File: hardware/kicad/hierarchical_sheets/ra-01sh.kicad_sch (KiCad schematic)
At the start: 3 parts, among them J4 CONSMA020.062-G, U3 RA-01SH

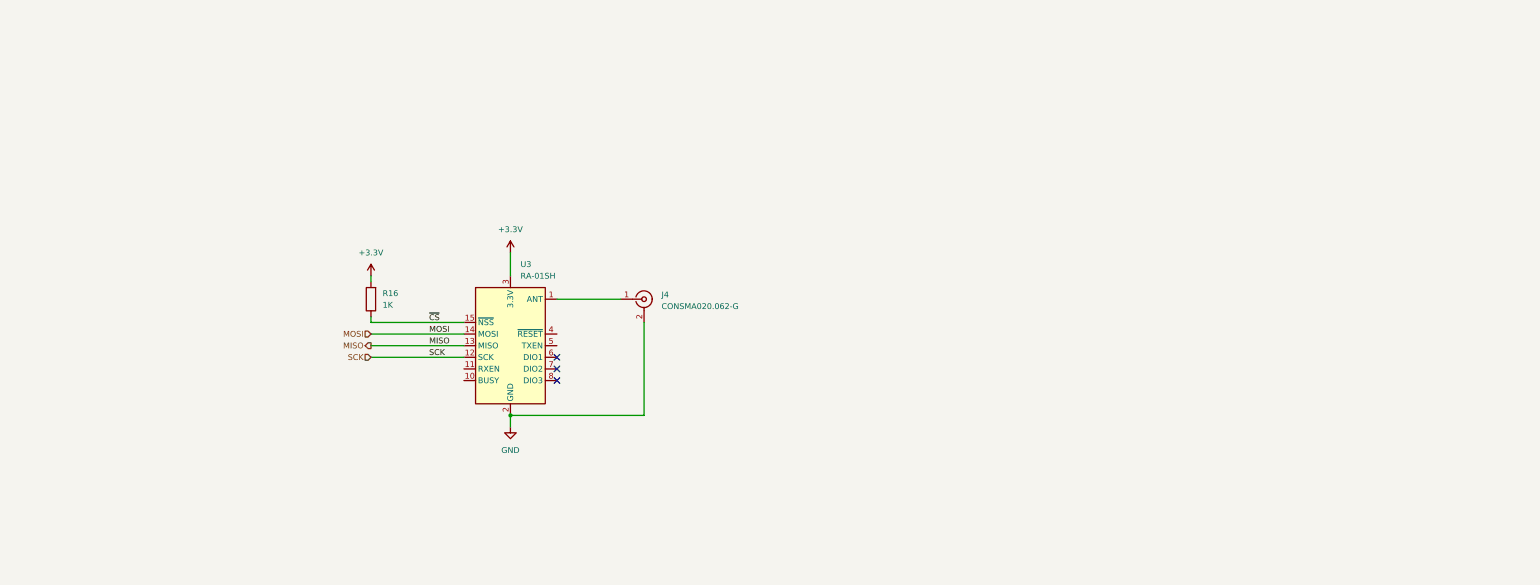
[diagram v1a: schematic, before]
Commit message: added comments to storage and telemetry radio
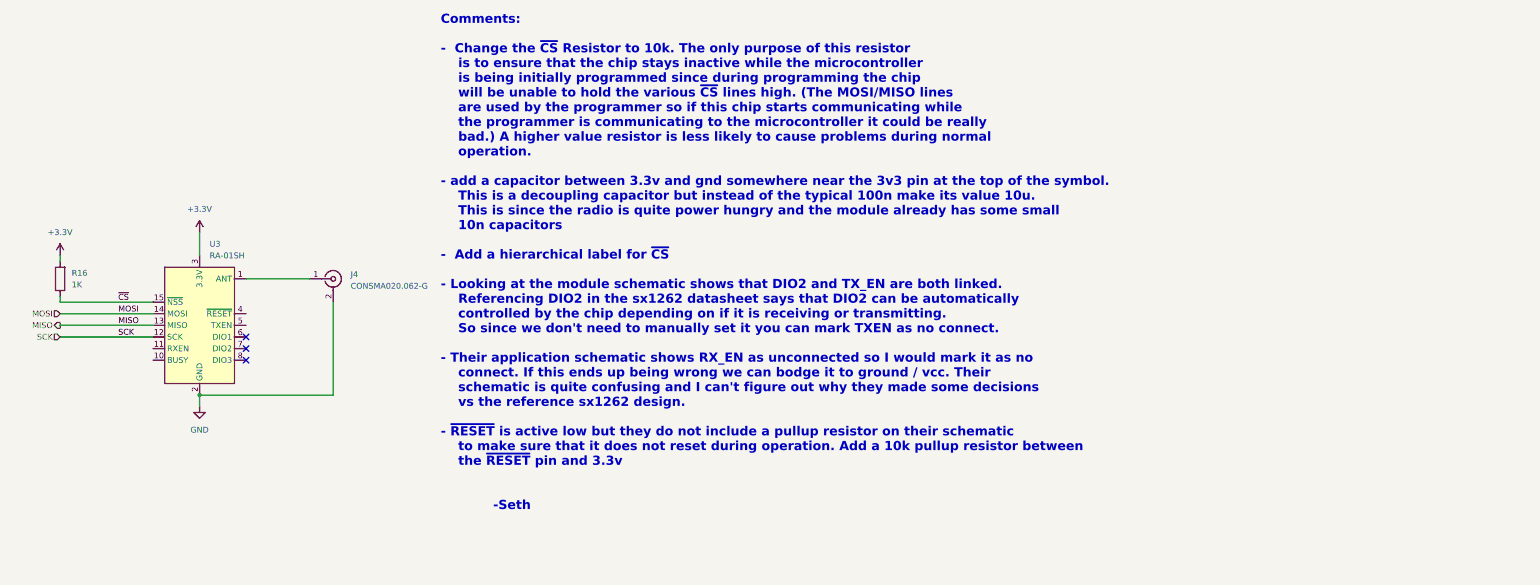
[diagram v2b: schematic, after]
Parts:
- U3: Digikey https://docs.ai-thinker.com/_media/lora/docs/ra-01sh_specif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 -> https://www.digikey.com/en/products/detail/ai-thinker/RA-01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
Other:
- note added: "Comments: - Change the ~{CS} Resistor to 10k. The only purpose of this resistor is to ensure that the chip stays inactive while the microcontroller is being initially programmed since during programming the chip will be unable to hold the various ~{CS} lines high. (The MOSI/MISO lines are used by the programmer so if this chip starts communicating while the programmer is communicating to the micr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"
- moved on the sheet: J4, R16, U3

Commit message: literally moved half the microcontroller pins :(
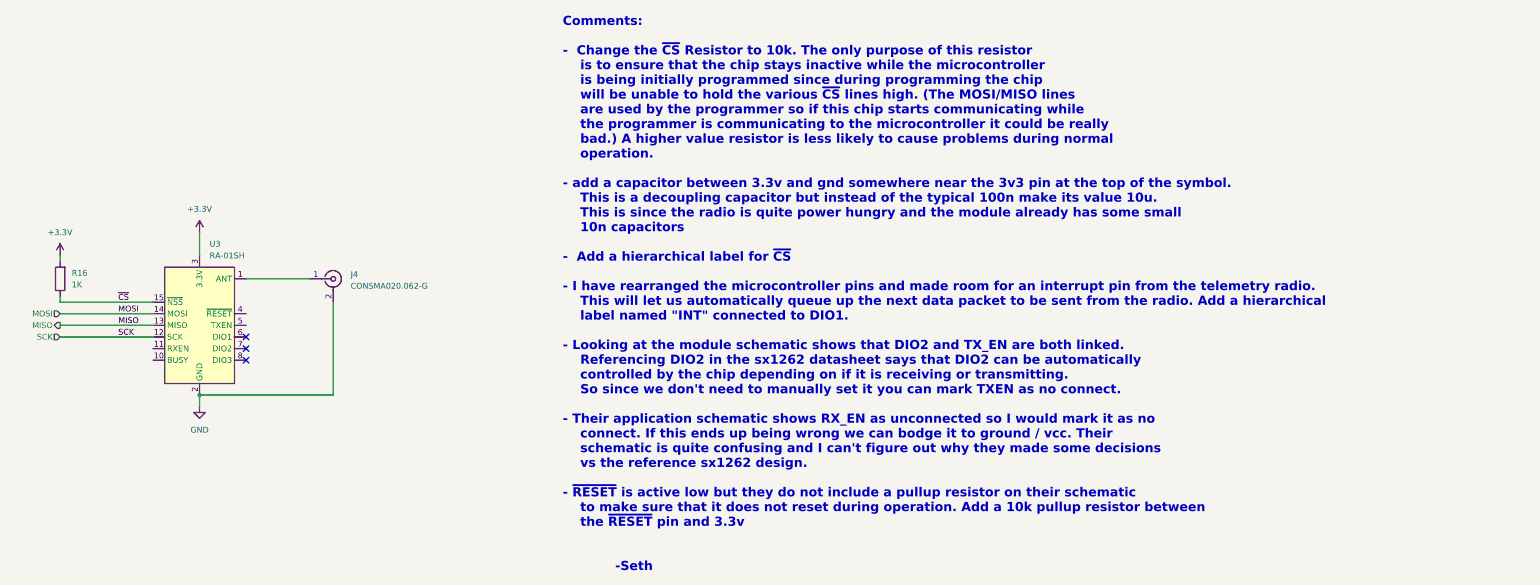
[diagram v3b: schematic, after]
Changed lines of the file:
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@@
     )
   )
-  (text "Comments:\n\n-  Change the ~{CS} Resistor to 10k. The only purpose of this resistor\n	is to ensure that the chip stays inactive while the microcontroller\n	is being initially programmed since during programming the chip\n	will be unable to hold the various ~{CS} lines high. (The MOSI/MISO lines \n	are used by the programmer so if this chip starts communicating while\n	the programmer is communicating to the microcontroller it could be really \n	bad.) A higher value resistor is less likely to cause problems during normal \n	operation. \n\n- add a capacitor between 3.3v and gnd somewhere near the 3v3 pin at the top of the symbol.\n	This is a decoupling capacitor but instead of the typical 100n make its value 10u.\n	This is since the radio is quite power hungry and the module already has some small\n	10n capacitors \n\n-  Add a hierarchical label for ~{CS} \n\n- Looking at the module schematic shows that DIO2 and TX_EN are both linked.\n	Referencing DIO2 in the sx1262 datasheet says that DIO2 can be automatically\n	controlled by the chip depending on if it is receiving or transmitting. \n	So since we don't need to manually set it you can mark TXEN as no connect. \n\n- Their application schematic shows RX_EN as unconnected so I would mark it as no \n	connect. If this ends up being wrong we can bodge it to ground / vcc. Their \n	schematic is quite confusing and I can't figure out why they made some decisions \n	vs the reference sx1262 design. \n\n- ~{RESET} is active low but they do not include a pullup resistor on their schematic\n	to make sure that it does not reset during operation. Add a 10k pullup resistor between \n	the ~{RESET} pin and 3.3v\n\n\n			-Seth"
-    (at 116.84 123.825 0)
+  (text "Comments:\n\n-  Change the ~{CS} Resistor to 10k. The only purpose of this resistor\n	is to ensure that the chip stays inactive while the microcontroller\n	is being initially programmed since during programming the chip\n	will be unable to hold the various ~{CS} lines high. (The MOSI/MISO lines \n	are used by the programmer so if this chip starts communicating while\n	the programmer is communicating to the microcontroller it could be really \n	bad.) A higher value resistor is less likely to cause problems during normal \n	operation. \n\n- add a capacitor between 3.3v and gnd somewhere near the 3v3 pin at the top of the symbol.\n	This is a decoupling capacitor but instead of the typical 100n make its value 10u.\n	This is since the radio is quite power hungry and the module already has some small\n	10n capacitors \n\n-  Add a hierarchical label for ~{CS} \n\n- I have rearranged the microcontroller pins and made room for an interrupt pin from the telemetry radio. \n	This will let us automatically queue up the next data packet to be sent from the radio. Add a hierarchical \n	label named \"INT\" connected to DIO1.\n\n- Looking at the module schematic shows that DIO2 and TX_EN are both linked.\n	Referencing DIO2 in the sx1262 datasheet says that DIO2 can be automatically\n	controlled by the chip depending on if it is receiving or transmitting. \n	So since we don't need to manually set it you can mark TXEN as no connect. \n\n- Their application schematic shows RX_EN as unconnected so I would mark it as no \n	connect. If this ends up being wrong we can bodge it to ground / vcc. Their \n	schematic is quite confusing and I can't figure out why they made some decisions \n	vs the reference sx1262 design. \n\n- ~{RESET} is active low but they do not include a pullup resistor on their schematic\n	to make sure that it does not reset during operation. Add a 10k pullup resistor between \n	the ~{RESET} pin and 3.3v\n\n\n			-Seth"
+    (at 143.51 137.16 0)
     (effects (font (size 2 2) (thickness 0.4) bold (color 255 48 0 1)) (justify left bottom))
   )

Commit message: fixed schematic RA-01SH
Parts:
- added C3: 100n, symbol Device:C
- added R22: 10k, symbol Device:R
- R16: value 1K -> 10K
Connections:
- net +3.3V: now also C3.1, R22.1
- net GND: now also C3.2
- net BUSY: now reaches U3.10 (BUSY)
- net at U3.4 (~{RESET}): now also R22.2
- net INT: now reaches U3.6 (DIO1)
- net ~{CS} renamed CS
- no-connect marks 3 -> 4
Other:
- note removed: "Comments: - Change the ~{CS} Resistor to 10k. The only purpose of this resistor is to ensure that the chip stays inactive while the microcontroller is being initially programmed since during programming the chip will be unable to hold the various ~{CS} lines high. (The MOSI/MISO lines are used by the programmer so if this chip starts communicating while the programmer is communicating to the micr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"

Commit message: Max Working Current
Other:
- note added: "Maximum Working Current is 140mA"
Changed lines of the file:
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@@
     )
+  )
+  (text "Maximum Working Current is 140mA" (at 48.26 120.65 0)
+    (effects (font (size 1.27 1.27)) (justify left bottom))
   )
   (label "MOSI" (at 46.355 80.645 0) (fields_autoplaced)

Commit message: added invert on cs
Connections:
- net CS renamed ~{CS}
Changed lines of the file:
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@@
     (effects (font (size 1.27 1.27)) (justify right))
   )
-  (hierarchical_label "CS" (shape input) (at 31.115 78.105 180) (fields_autoplaced)
+  (hierarchical_label "~{CS}" (shape input) (at 31.115 78.105 180) (fields_autoplaced)
     (effects (font (size 1.27 1.27)) (justify right))
   )

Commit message: added power and checked schematics
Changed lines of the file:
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@@
     (effects (font (size 1.27 1.27)) (justify right))
   )
-  (hierarchical_label "INT" (shape input) (at 80.01 85.725 0) (fields_autoplaced)
+  (hierarchical_label "INT" (shape output) (at 80.01 85.725 0) (fields_autoplaced)
     (effects (font (size 1.27 1.27)) (justify left))
   )

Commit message: assigned footprints
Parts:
- C7: renamed from C3; footprint (none) -> Resistor_SMD:R_0603_1608Metric
- R16: footprint (none) -> Resistor_SMD:R_0603_1608Metric
- R17: renamed from R22; footprint (none) -> Resistor_SMD:R_0603_1608Metric
- renumbered U3 to U6
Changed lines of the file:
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@@
   (symbol (lib_id "power:GND") (at 49.53 64.77 0) (unit 1)
     (in_bom yes) (on_board yes) (dnp no) (fields_autoplaced)
-    (property "Reference" "#PWR028" (at 49.53 71.12 0)
+    (property "Reference" "#PWR027" (at 49.53 71.12 0)
       (effects (font (size 1.27 1.27)) hide)
     )
@@
       (project "FC"
         (path "/54cce219-8b98-4e71-96c4-f9ee784aa3bc/35031a3a-251a-4009-92bf-5738de5c8c69"
+          (reference "#PWR027") (unit 1)
+        )
+      )
+    )
+  )
+  (symbol (lib_id "power:GND") (at 64.135 100.965 0) (unit 1)
+    (in_bom yes) (on_board yes) (dnp no) (fields_autoplaced)
+    (property "Reference" "#PWR028" (at 64.135 107.315 0)
+      (effects (font (size 1.27 1.27)) hide)
+    )
+    (property "Value" "GND" (at 64.135 106.045 0)
+      (effects (font (size 1.27 1.27)))
+    )
+    (property "Footprint" "" (at 64.135 100.965 0)
+      (effects (font (size 1.27 1.27)) hide)
+    )
+    (property "Datasheet" "" (at 64.135 100.965 0)
+      (effects (font (size 1.27 1.27)) hide)
+    )
+    (pin "1")
+    (instances
+      (project "FC"
+        (path "/54cce219-8b98-4e71-96c4-f9ee784aa3bc/35031a3a-251a-4009-92bf-5738de5c8c69"
           (reference "#PWR028") (unit 1)
         )
@@
     )
   )
-  (symbol (lib_id "power:GND") (at 64.135 100.965 0) (unit 1)
-    (in_bom yes) (on_board yes) (dnp no) (fields_autoplaced)
-    (property "Reference" "#PWR024" (at 64.135 107.315 0)
-      (effects (font (size 1.27 1.27)) hide)
-    )
-    (property "Value" "GND" (at 64.135 106.045 0)
-      (effects (font (size 1.27 1.27)))
-    )
-    (property "Footprint" "" (at 64.135 100.965 0)
-      (effects (font (size 1.27 1.27)) hide)
-    )
-    (property "Datasheet" "" (at 64.135 100.965 0)
-      (effects (font (size 1.27 1.27)) hide)
-    )
-    (pin "1")
-    (instances
-      (project "FC"
-        (path "/54cce219-8b98-4e71-96c4-f9ee784aa3bc/35031a3a-251a-4009-92bf-5738de5c8c69"
-          (reference "#PWR024") (unit 1)
-        )
-      )
-    )
-  )
   (symbol (lib_id "Device:R") (at 133.985 62.23 0) (unit 1)
     (in_bom yes) (on_board yes) (dnp no) (fields_autoplaced)
-    (property "Reference" "R22" (at 135.89 60.96 0)
+    (property "Reference" "R17" (at 135.89 60.96 0)
       (effects (font (size 1.27 1.27)) (justify left))
     )
@@
       (effects (font (size 1.27 1.27)) (justify left))
     )
-    (property "Footprint" "" (at 132.207 62.23 90)
+    (property "Footprint" "Resistor_SMD:R_0603_1608Metric" (at 132.207 62.23 90)
       (effects (font (size 1.27 1.27)) hide)
     )
@@
       (project "FC"
         (path "/54cce219-8b98-4e71-96c4-f9ee784aa3bc/35031a3a-251a-4009-92bf-5738de5c8c69"
-          (reference "R22") (unit 1)
+          (reference "R17") (unit 1)
         )
       )
@@
   (symbol (lib_id "Device:C") (at 49.53 58.42 0) (unit 1)
     (in_bom yes) (on_board yes) (dnp no) (fields_autoplaced)
-    (property "Reference" "C3" (at 53.34 57.15 0)
+    (property "Reference" "C7" (at 53.34 57.15 0)
       (effects (font (size 1.27 1.27)) (justify left))
     )
@@
       (effects (font (size 1.27 1.27)) (justify left))
     )
-    (property "Footprint" "" (at 50.4952 62.23 0)
+    (property "Footprint" "Resistor_SMD:R_0603_1608Metric" (at 50.4952 62.23 0)
       (effects (font (size 1.27 1.27)) hide)
     )
@@
       (project "FC"
         (path "/54cce219-8b98-4e71-96c4-f9ee784aa3bc/35031a3a-251a-4009-92bf-5738de5c8c69"
-          (reference "C3") (unit 1)
+          (reference "C7") (unit 1)
         )
       )
@@
   (symbol (lib_id "RA-01SH:RA-01SH") (at 64.135 83.185 0) (unit 1)
     (in_bom yes) (on_board yes) (dnp no) (fields_autoplaced)
-    (property "Reference" "U3" (at 66.3291 65.405 0)
+    (property "Reference" "U6" (at 66.3291 65.405 0)
       (effects (font (size 1.27 1.27)) (justify left))
     )
@@
       (project "FC"
         (path "/54cce219-8b98-4e71-96c4-f9ee784aa3bc/35031a3a-251a-4009-92bf-5738de5c8c69"
-          (reference "U3") (unit 1)
+          (reference "U6") (unit 1)
         )
       )
@@
       (effects (font (size 1.27 1.27)) (justify right))
     )
-    (property "Footprint" "" (at 35.433 73.025 90)
+    (property "Footprint" "Resistor_SMD:R_0603_1608Metric" (at 35.433 73.025 90)
       (effects (font (size 1.27 1.27)) hide)
     )
@@
   (symbol (lib_id "power:+3.3V") (at 46.99 48.26 0) (unit 1)
     (in_bom yes) (on_board yes) (dnp no) (fields_autoplaced)
-    (property "Reference" "#PWR022" (at 46.99 52.07 0)
+    (property "Reference" "#PWR026" (at 46.99 52.07 0)
       (effects (font (size 1.27 1.27)) hide)
     )
@@
       (project "FC"
         (path "/54cce219-8b98-4e71-96c4-f9ee784aa3bc/35031a3a-251a-4009-92bf-5738de5c8c69"
-          (reference "#PWR022") (unit 1)
+          (reference "#PWR026") (unit 1)
         )
       )
@@
   (symbol (lib_id "power:+3.3V") (at 33.655 67.945 0) (unit 1)
     (in_bom yes) (on_board yes) (dnp no) (fields_autoplaced)
-    (property "Reference" "#PWR023" (at 33.655 71.755 0)
+    (property "Reference" "#PWR025" (at 33.655 71.755 0)
       (effects (font (size 1.27 1.27)) hide)
     )
@@
       (project "FC"
         (path "/54cce219-8b98-4e71-96c4-f9ee784aa3bc/35031a3a-251a-4009-92bf-5738de5c8c69"
-          (reference "#PWR023") (unit 1)
-        )
-      )
+          (reference "#PWR025") (unit 1)
+        )
+      )
